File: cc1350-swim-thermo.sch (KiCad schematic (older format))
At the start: 1 part

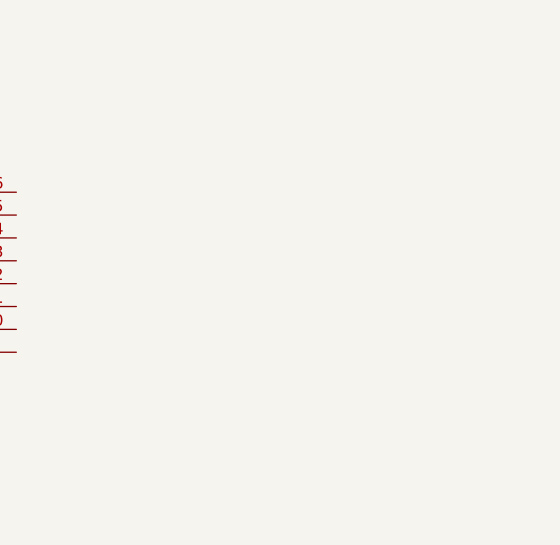
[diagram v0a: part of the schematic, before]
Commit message: added rf switch
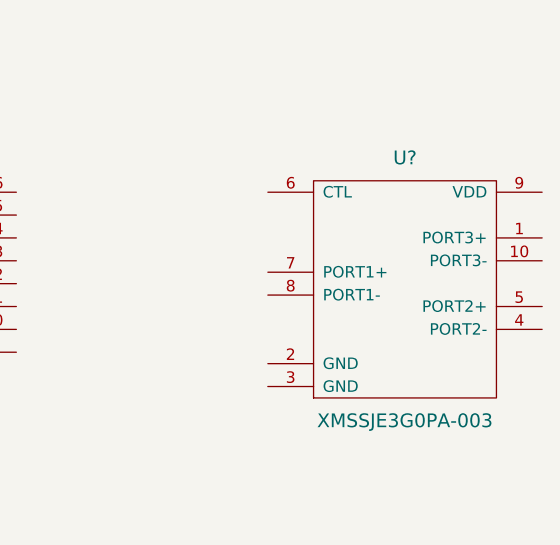
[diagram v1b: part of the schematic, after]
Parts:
- added U?: XMSSJE3G0PA-003, symbol XMSSJE3G0PA-003
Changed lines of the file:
@@
 LIBS:valves
 LIBS:cc1350
+LIBS:cc1350-swim-thermo-cache
 EELAYER 25 0
 EELAYER END
@@
 	1    0    0    -1
 $EndComp
+$Comp
+L XMSSJE3G0PA-003 U?
+U 1 1 58BEE092
+P 8350 3450
+F 0 "U?" H 8350 4000 60  0000 C CNN
+F 1 "XMSSJE3G0PA-003" H 8350 2850 60  0000 C CNN
+F 2 "" H 8200 3050 60  0001 C CNN
+F 3 "" H 8200 3050 60  0001 C CNN
+	1    8350 3450
+	1    0    0    -1
+$EndComp

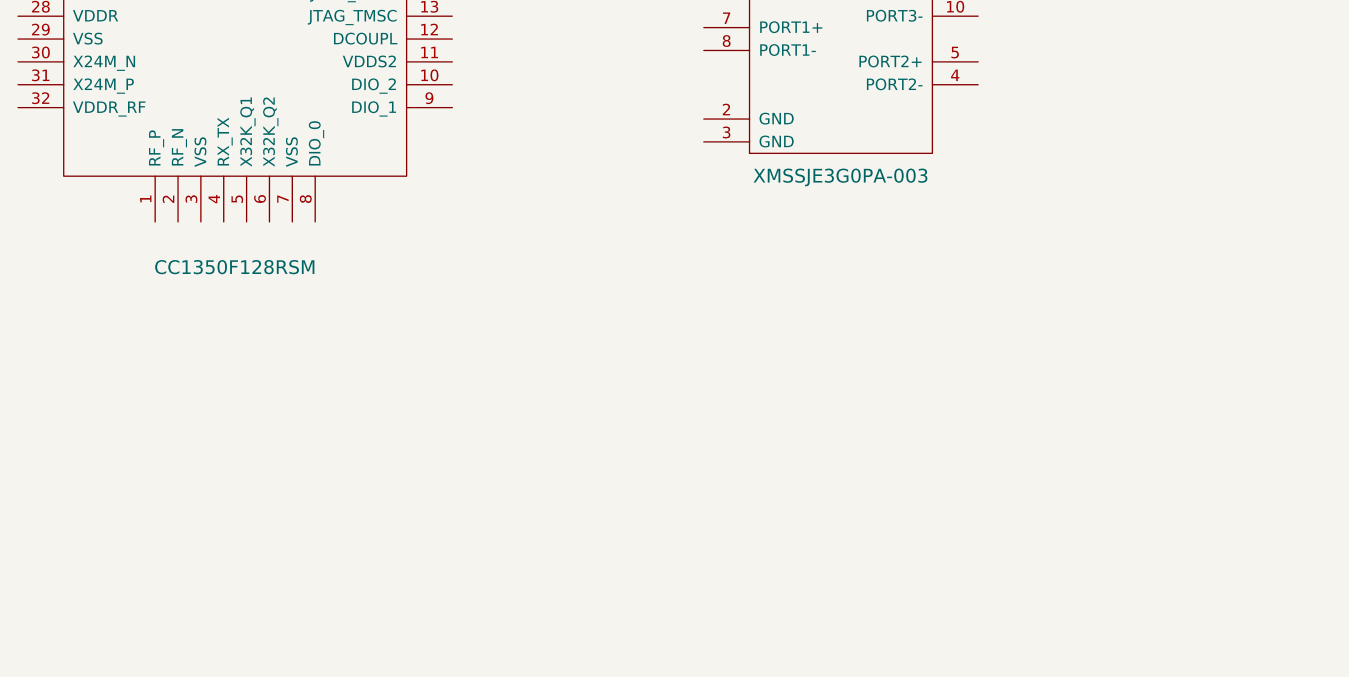
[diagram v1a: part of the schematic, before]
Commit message: added schema symbols
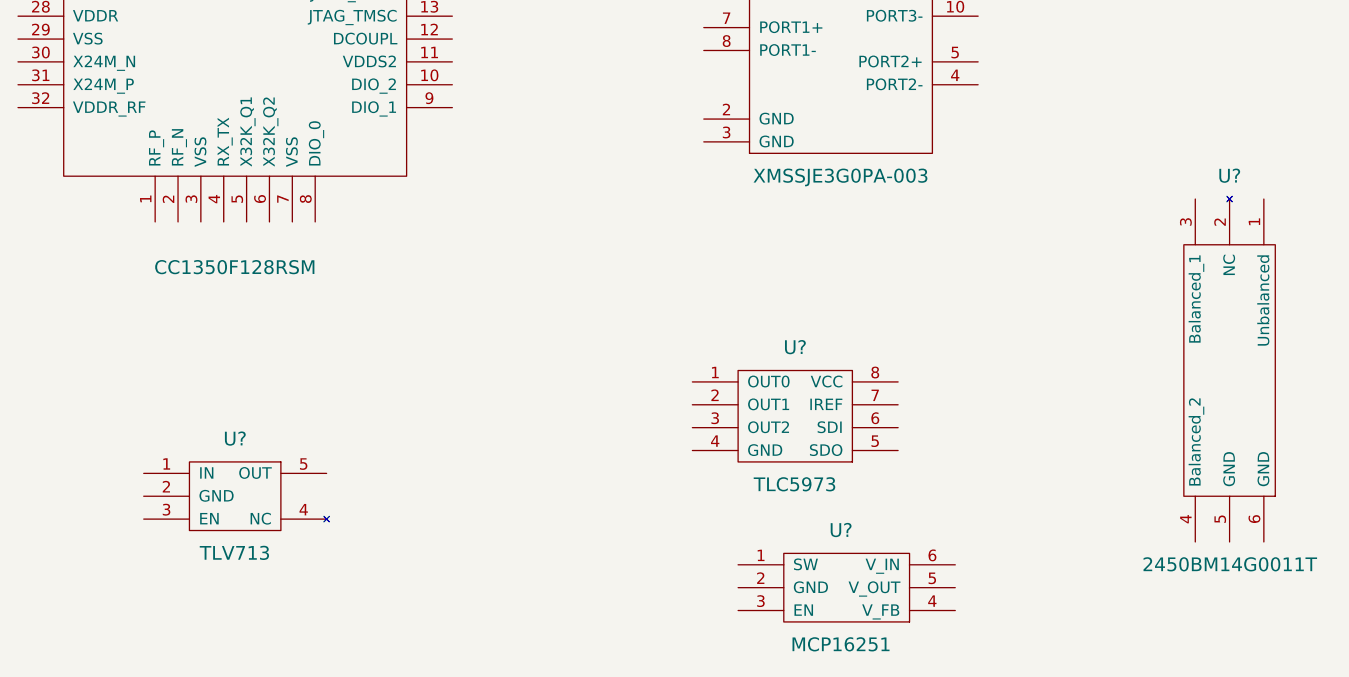
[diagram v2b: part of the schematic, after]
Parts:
- added U?: 2450BM14G0011T, symbol 2450BM14G0011T
- added U?: TLC5973, symbol TLC5973
- added U?: MCP16251, symbol MCP16251
- added U?: TLV713, symbol TLV713
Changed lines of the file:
@@
+	1    0    0    -1
+$EndComp
+$Comp
+L 2450BM14G0011T U?
+U 1 1 58C05583
+P 10050 4900
+F 0 "U?" H 10050 5750 60  0000 C CNN
+F 1 "2450BM14G0011T" H 10050 4050 60  0000 C CNN
+F 2 "" H 9850 4900 60  0001 C CNN
+F 3 "" H 9850 4900 60  0001 C CNN
+	1    10050 4900
+	1    0    0    -1
+$EndComp
+$Comp
+L TLC5973 U?
+U 1 1 58C057CB
+P 8150 5100
+F 0 "U?" H 8150 5400 60  0000 C CNN
+F 1 "TLC5973" H 8150 4800 60  0000 C CNN
+F 2 "" H 8150 5100 60  0001 C CNN
+F 3 "" H 8150 5100 60  0001 C CNN
+	1    8150 5100
+	1    0    0    -1
+$EndComp
+$Comp
+L MCP16251 U?
+U 1 1 58C05985
+P 8350 5850
+F 0 "U?" H 8350 6100 60  0000 C CNN
+F 1 "MCP16251" H 8350 5600 60  0000 C CNN
+F 2 "" H 8350 5850 60  0001 C CNN
+F 3 "" H 8350 5850 60  0001 C CNN
+	1    8350 5850
+	1    0    0    -1
+$EndComp
+$Comp
+L TLV713 U?
+U 1 1 58C05C42
+P 5700 5450
+F 0 "U?" H 5700 5700 60  0000 C CNN
+F 1 "TLV713" H 5700 5200 60  0000 C CNN
+F 2 "" H 5700 5250 60  0001 C CNN
+F 3 "" H 5700 5250 60  0001 C CNN
+	1    5700 5450
 	1    0    0    -1
 $EndComp

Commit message: schema for rf section
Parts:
- added AE?: Antenna_Shield, symbol Antenna_Shield
- added C? (x6): 12pF, symbol C
- added C? (x2): 3.6pF, symbol C
- added C?: 3pF, symbol C
- added C?: 6.8pF, symbol C
- added C?: 3.3pF, symbol C
- added C?: 100pF, symbol C
- added L? (x2): 10nH, symbol L
- added L? (x4): 6.8nH, symbol L
- added P?: BNC, symbol BNC
- added U?: 2450BM14G0011T, symbol 2450BM14G0011T
- added Y?: 32.768kHz, symbol Crystal
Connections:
- net at U?.1 (RF_P): now also C?.2, L?.1
- net at U?.2 (RF_N): now also C?.2, L?.1
- net GND: now reaches U?.3 (VSS)
- net GND: now also U?.2 (GND), U?.3 (GND), U?.7 (VSS), AE?.2 (Shield), C?.1, C?.2, C?.2, C?.2, C?.2, C?.2, C?.2, C?.2, L?.1, P?.2 (Ext), U?.5 (GND), U?.6 (GND)
- net at U?.4 (RX_TX): now also C?.1, C?.1, L?.2, L?.2
- net at U?.5 (X32K_Q1): now also C?.1, Y?.1
- net at U?.6 (X32K_Q2): now also C?.1, Y?.2
- net DIO0_RF_SW_PWR: now reaches U?.8 (DIO_0)
- net DIO0_RF_SW_PWR: now also U?.9 (VDD)
- net DIO1_RF_SW: now reaches U?.9 (DIO_1)
- net DIO1_RF_SW: now also U?.6 (CTL)
- net at U?.1 (PORT3+): now also C?.2, L?.2
- net at U?.10 (PORT3-): now also C?.2, L?.2
- net at U?.4 (PORT2-): now also U?.4 (Balanced_2)
- net at U?.5 (PORT2+): now also U?.3 (Balanced_1)
- net at U?.7 (PORT1+): now also C?.1
- net at U?.8 (PORT1-): now also C?.1
- new net: AE?.1 (A), U?.1 (Unbalanced)
- new net: C?.1, C?.1, L?.1, L?.2
- new net: C?.1, L?.1, L?.2
- new net: C?.1, C?.2, L?.1
- new net: C?.1, P?.1 (In)
- no-connect marks 0 -> 2
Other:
- moved on the sheet: U?

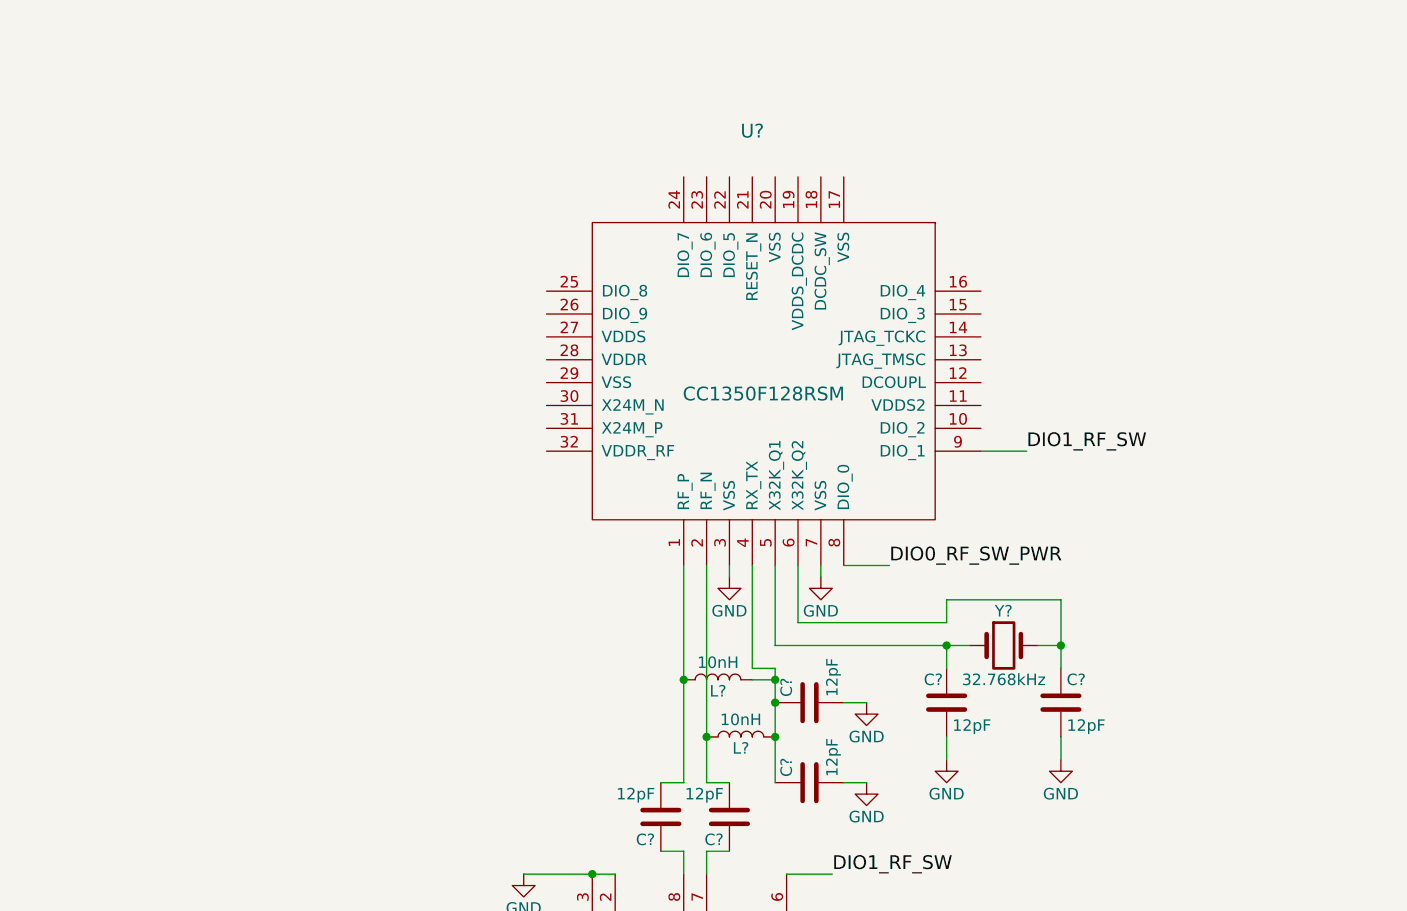
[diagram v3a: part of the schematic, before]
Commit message: voltage supply rails schema
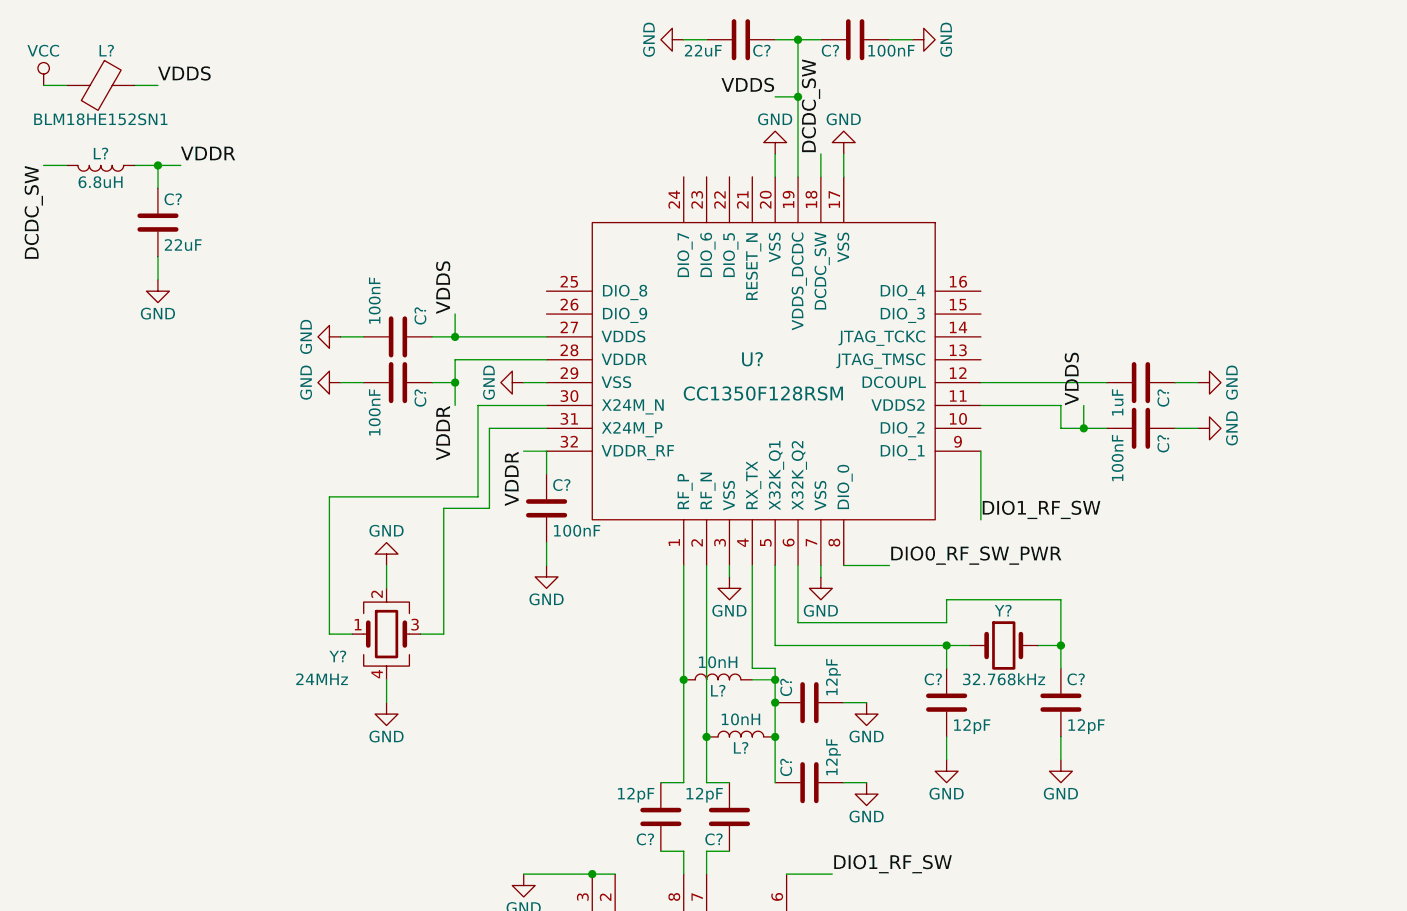
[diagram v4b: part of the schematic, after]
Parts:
- added C? (x5): 100nF, symbol C
- added C? (x2): 22uF, symbol C
- added C?: 1uF, symbol C
- added L?: BLM18HE152SN1, symbol Ferrite_Bead
- added L?: 6.8uH, symbol L
- added Y?: 24MHz, symbol Crystal_GND24
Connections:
- net GND: now also U?.17 (VSS), U?.20 (VSS), U?.29 (VSS), C?.1, C?.1, C?.1, C?.1, C?.2, C?.2, C?.2, C?.2, Y?.2, Y?.4
- net VDDS: now reaches U?.11 (VDDS2)
- net VDDS: now also U?.19 (VDDS_DCDC), U?.27 (VDDS), C?.1, C?.2, C?.2, C?.2, L?.1
- net at U?.12 (DCOUPL): now also C?.2
- net DCDC_SW: now reaches U?.18 (DCDC_SW)
- net DCDC_SW: now also L?.2
- net VDDR: now reaches U?.28 (VDDR)
- net VDDR: now also U?.32 (VDDR_RF), C?.1, C?.1, C?.1, L?.1
- net at U?.30 (X24M_N): now also Y?.1
- net at U?.31 (X24M_P): now also Y?.3
- new net VCC: L?.2

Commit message: external components
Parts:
- removed U?: 2450BM14G0011T, symbol 2450BM14G0011T
- added BT?: Battery, symbol Battery
- added C?: 4.7uF, symbol C
- added C?: 10uF, symbol C
- added C? (x3): 100nF, symbol C
- added D?: CLV1A-FKB, symbol LED_ARGB
- added L?: 4.7uH, symbol L
- added L?: BLM18HE152SN1, symbol Ferrite_Bead
- added P?: USB_OTG, symbol USB_OTG
- added Q?: 2N7002, symbol Q_NMOS_GSD
- added R?: 1M, symbol R
- added R?: 3.09M, symbol R
- added R? (x2): 10K, symbol R
- added R?: 2.08K, symbol R
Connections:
- net GND: now also U?.2 (GND), U?.2 (GND), U?.4 (GND), BT?.2 (-), C?.1, C?.1, C?.2, C?.2, C?.2, P?.5 (GND), P?.6 (shield), Q?.2 (S), R?.1, R?.2, R?.2
- net VCC: now also U?.5 (OUT), U?.6 (V_IN), BT?.1 (+), C?.1, C?.2, L?.2
- net PSU_ENABLE: now reaches U?.10 (DIO_2)
- net PSU_ENABLE: now also U?.3 (EN), R?.1
- net LED_EASYSET: now reaches U?.15 (DIO_3)
- net LED_EASYSET: now also Q?.1 (G)
- net at U?.1 (OUT0): now also D?.4 (BK)
- net at U?.2 (OUT1): now also D?.3 (GK)
- net at U?.3 (OUT2): now also D?.2 (RK)
- net at U?.6 (SDI): now also Q?.3 (D), R?.2
- net at U?.7 (IREF): now also R?.2
- net +5V: now reaches U?.8 (VCC)
- net +5V: now also U?.5 (V_OUT), C?.1, C?.1, D?.1 (A), R?.1, R?.1
- net at U?.1 (SW): now also L?.1
- net at U?.4 (V_FB): now also R?.1, R?.2
- net at U?.1 (IN): now also U?.3 (EN), C?.2, L?.1
- new net: L?.2, P?.1 (VBUS)
- no-connect marks 2 -> 7
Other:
- note added: "Device uses either USB or battery power. \nIf battery power no USB or LDO is mounted."
- note added: "For I=25mA"
- moved on the sheet: U?

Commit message: added JTAG
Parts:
- added C?: 100nF, symbol C
- added P?: CONN_02X05, symbol CONN_02X05
- added R?: 100K, symbol R
- C?: value 100nF -> 1uF
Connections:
- net GND: now also C?.2, P?.3 (P3), P?.5 (P5), P?.9 (P9)
- net LED_EASYSET: now also U?.26 (DIO_9); no longer U?.15 (DIO_3)
- net VCC: now also P?.1 (P1)
- net VDDS: now also R?.1
- net JTAG_TMSC: now reaches U?.13 (JTAG_TMSC)
- net JTAG_TCKC: now reaches U?.14 (JTAG_TCKC)
- net JTAG_TDI: now reaches U?.16 (DIO_4)
- net JTAG_TDI: now also P?.8 (P8)
- net RESET_N: now reaches U?.21 (RESET_N)
- net RESET_N: now also C?.1, P?.10 (P10), R?.2
- new net JTAG_TCK: P?.4 (P4)
- new net JTAG_TDO: P?.6 (P6), U?.15 (DIO_3)
- new net JTAG_TMS: P?.2 (P2)
- no-connect marks 7 -> 8
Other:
- note added: "5V PSU (for LEDs etc)"
- note added: "JTAG - Matching CC1350 Launchpad"
- note added: "LED Driver"

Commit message: tidying up
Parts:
- added JP?: Jumper_NC, symbol Jumper_NC_Small
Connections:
- net VCC: now also JP?.1; no longer BT?.1 (+)
- new net: BT?.1 (+), JP?.2
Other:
- note added: "868MHz RF section"
- note added: "BLE RF section"
- note added: "Remove jumper \nfor programming"
- moved on the sheet: AE?, BT?, C?, D?, L?, P?, Q?, R?, U?, Y?

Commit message: schema v1 ready
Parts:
- added P1: LMT_70_1, symbol CONN_01X04
- added P2: LMT_70_2, symbol CONN_01X04
- added R1: 100, symbol R
- added SW1: SW_Push, symbol SW_Push
- gave numbers to parts that had none: 58
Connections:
- net JTAG_TCK is gone; now on net JTAG_TCKC: P5.4 (P4)
- net JTAG_TMS is gone; now on net JTAG_TMSC: P5.2 (P2)
- net GND: now also P1.2 (P2), P2.2 (P2), SW1.1
- net VCC: now also P1.1 (P1), P2.1 (P1)
- net T_ON_1: now reaches U3.22 (DIO_5)
- net T_ON_1: now also P1.4 (P4)
- net T_ON_2: now reaches U3.23 (DIO_6)
- net T_ON_2: now also P2.4 (P4)
- net TAO: now reaches U3.24 (DIO_7)
- net TAO: now also P1.3 (P3), P2.3 (P3)
- net SWITCH: now reaches U3.25 (DIO_8)
- net SWITCH: now also R1.1
- new net: R1.2, SW1.2
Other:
- moved on the sheet: BT1, C18, C21, C23, C3, JP1, L6, L7, U4
